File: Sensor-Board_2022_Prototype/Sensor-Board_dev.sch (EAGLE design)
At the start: 21 parts

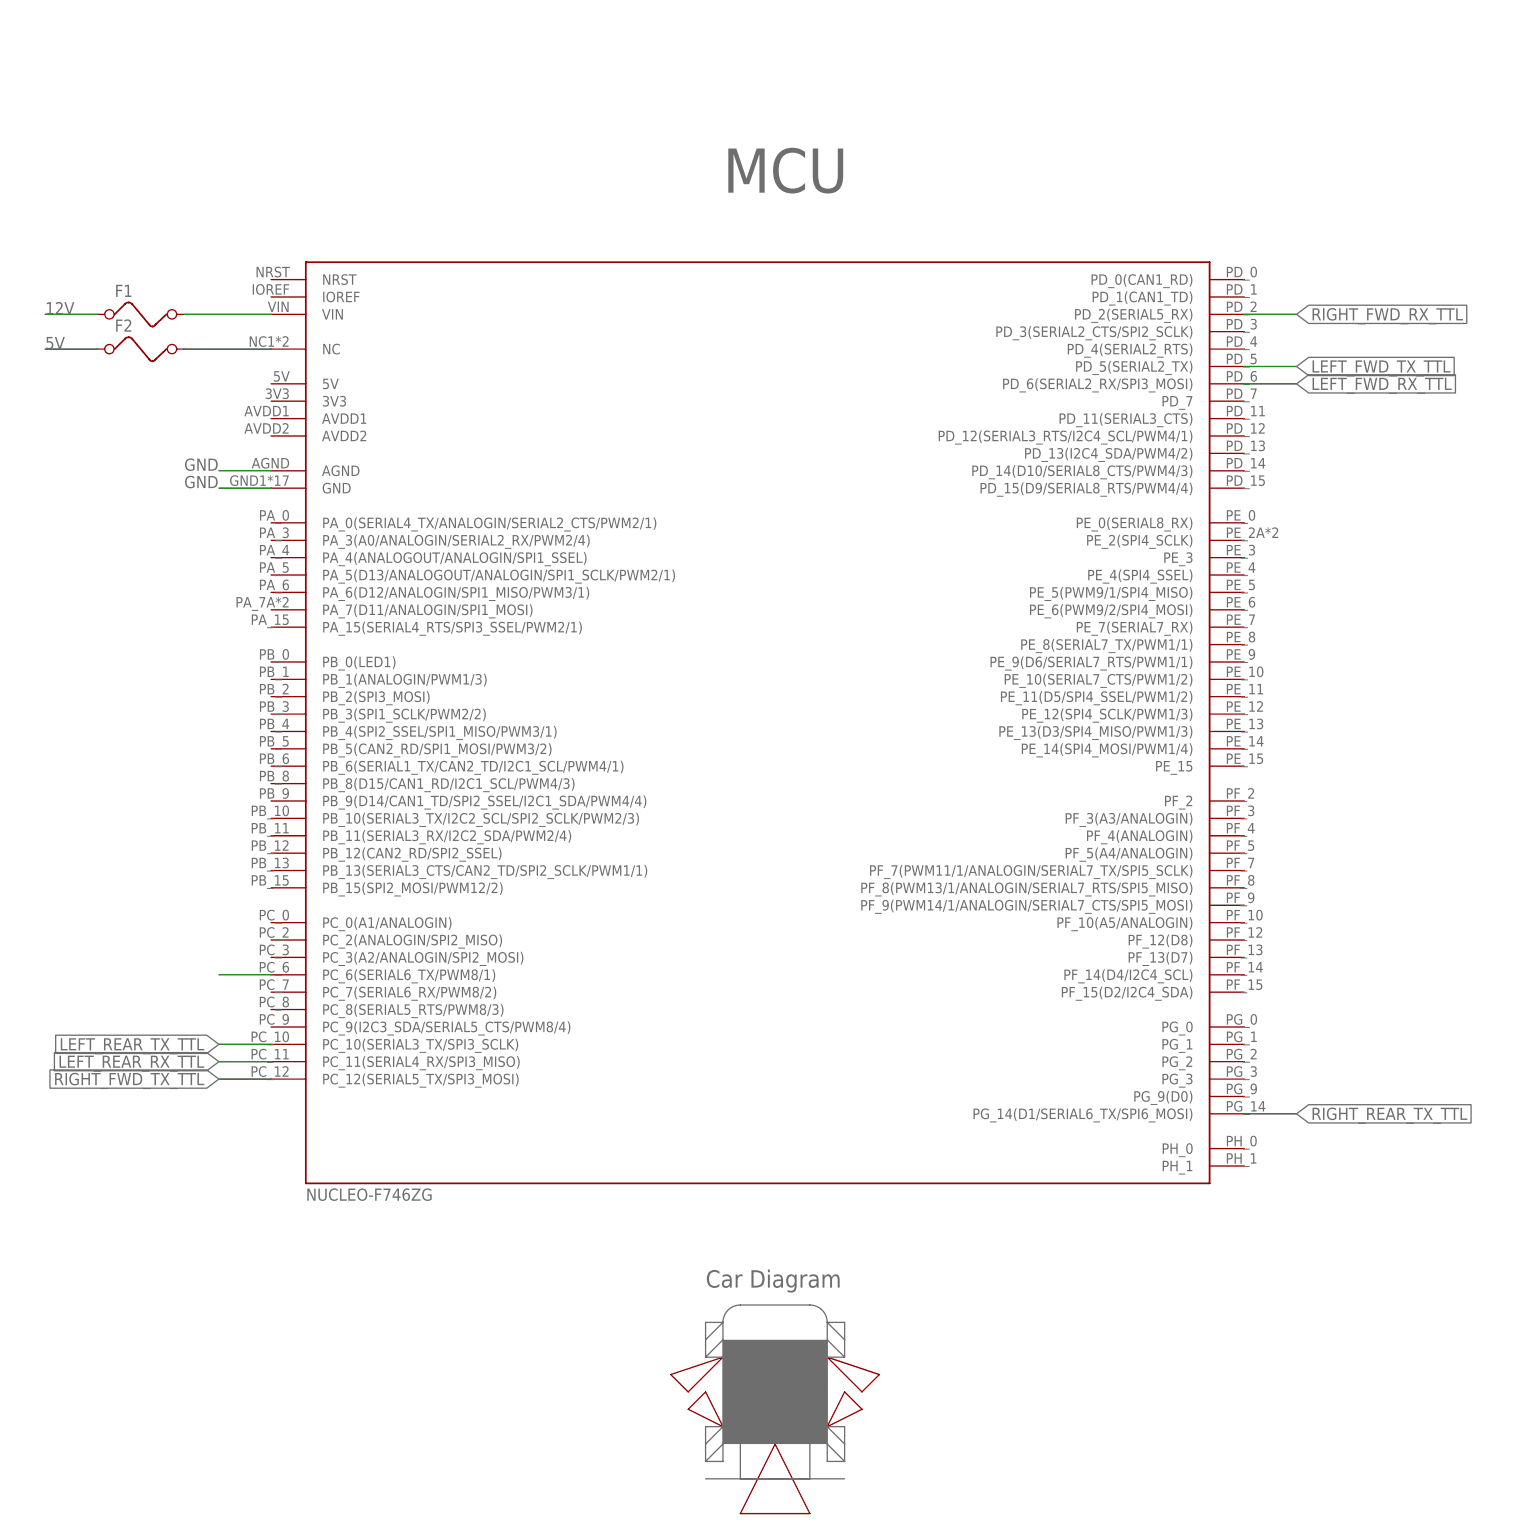
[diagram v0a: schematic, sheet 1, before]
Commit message: Added side signal labels
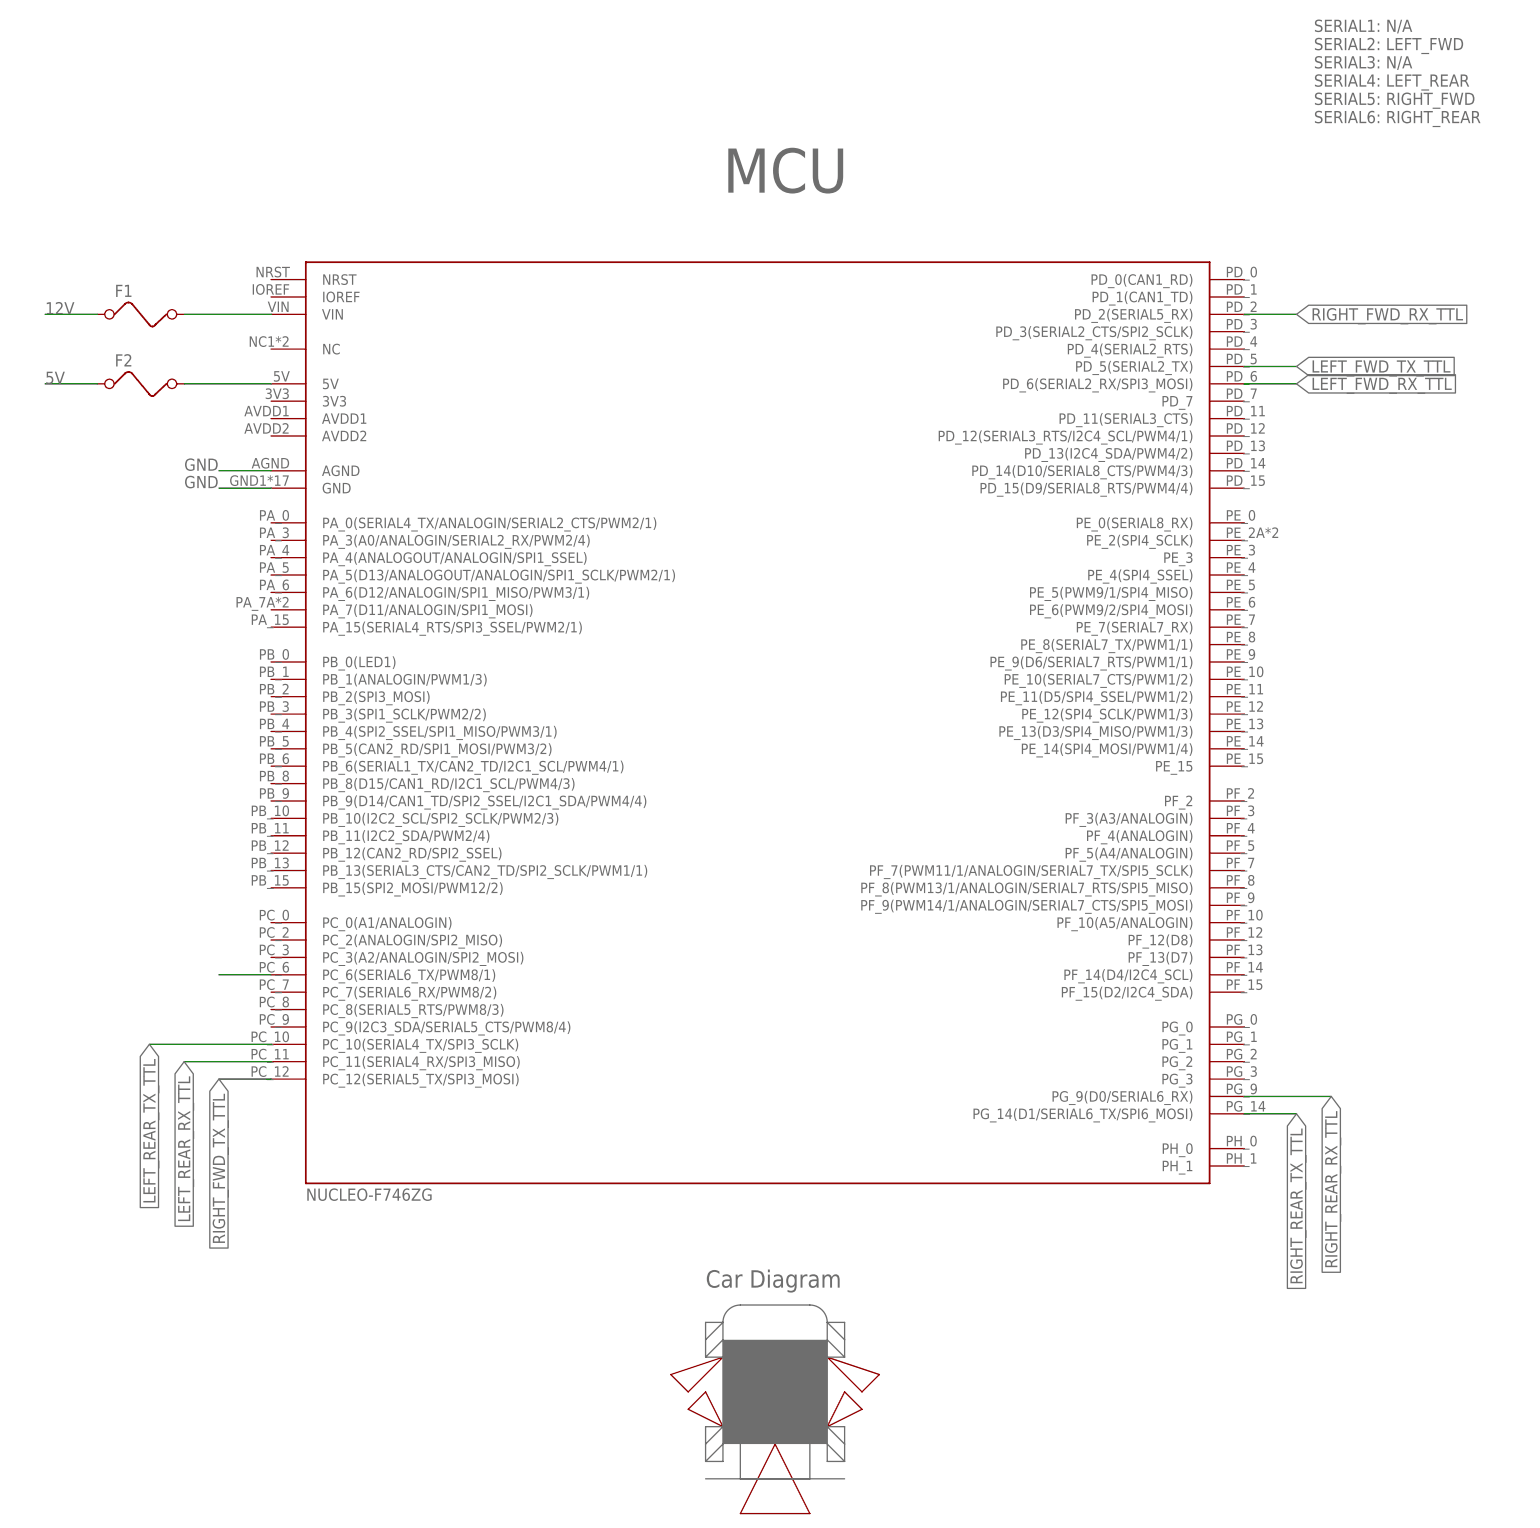
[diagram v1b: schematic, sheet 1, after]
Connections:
- net LEFT_REAR_TX_TTL: now also UC1.PC_10(SERIAL4_TX/SPI3_SCLK); no longer UC1.PC_10(SERIAL3_TX/SPI3_SCLK)
- net N$9: now also UC1.5V; no longer UC1.NC
- net RIGHT_REAR_RX_TTL: now also UC1.PG_9(D0/SERIAL6_RX)
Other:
- note added: "SERIAL1: N/A SERIAL2: LEFT_FWD SERIAL3: N/A SERIAL4: LEFT_REAR SERIAL5: RIGHT_FWD SERIAL6: RIGHT_REAR"
- moved on the sheet: F2
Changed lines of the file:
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@@
 <wire x1="160.02" y1="-5.08" x2="157.48" y2="-7.62" width="0.1524" layer="94"/>
 <text x="134.62" y="7.62" size="2.54" layer="95">Car Diagram</text>
+<text x="223.52" y="177.8" size="1.778" layer="95">SERIAL1: N/A
+SERIAL2: LEFT_FWD
+SERIAL3: N/A
+SERIAL4: LEFT_REAR
+SERIAL5: RIGHT_FWD
+SERIAL6: RIGHT_REAR</text>
 </plain>
 <instances>
@@
 <attribute name="VALUE" x="48.26" y="146.05" size="1.778" layer="96"/>
 </instance>
-<instance part="F2" gate="G$1" x="53.34" y="144.78" smashed="yes">
-<attribute name="NAME" x="48.26" y="147.32" size="1.778" layer="95"/>
-<attribute name="VALUE" x="48.26" y="140.97" size="1.778" layer="96"/>
+<instance part="F2" gate="G$1" x="53.34" y="139.7" smashed="yes">
+<attribute name="NAME" x="48.26" y="142.24" size="1.778" layer="95"/>
+<attribute name="VALUE" x="48.26" y="135.89" size="1.778" layer="96"/>
 </instance>
 <instance part="FRAME2" gate="G$1" x="-66.04" y="-58.42" smashed="yes"/>
@@
 <segment>
 <pinref part="F2" gate="G$1" pin="1"/>
-<wire x1="45.72" y1="144.78" x2="38.1" y2="144.78" width="0.1524" layer="91"/>
-<label x="38.1" y="144.78" size="1.778" layer="95"/>
+<wire x1="45.72" y1="139.7" x2="38.1" y2="139.7" width="0.1524" layer="91"/>
+<label x="38.1" y="139.7" size="1.778" layer="95"/>
 </segment>
 </net>
@@
 </segment>
 </net>
-<net name="N$9" class="0">
-<segment>
-<pinref part="UC1" gate="G$1" pin="NC"/>
-<wire x1="71.12" y1="144.78" x2="58.42" y2="144.78" width="0.1524" layer="91"/>
-<pinref part="F2" gate="G$1" pin="2"/>
-</segment>
-</net>
 <net name="LEFT_FWD_RX_TTL" class="0">
 <segment>
@@
 <segment>
 <pinref part="UC1" gate="G$1" pin="PC_11(SERIAL4_RX/SPI3_MISO)"/>
-<wire x1="71.12" y1="40.64" x2="63.5" y2="40.64" width="0.1524" layer="91"/>
-<label x="63.5" y="40.64" size="1.778" layer="95" rot="R180" xref="yes"/>
+<wire x1="71.12" y1="40.64" x2="58.42" y2="40.64" width="0.1524" layer="91"/>
+<label x="58.42" y="40.64" size="1.778" layer="95" rot="R270" xref="yes"/>
 </segment>
 </net>
 <net name="LEFT_REAR_TX_TTL" class="0">
 <segment>
-<pinref part="UC1" gate="G$1" pin="PC_10(SERIAL3_TX/SPI3_SCLK)"/>
-<wire x1="71.12" y1="43.18" x2="63.5" y2="43.18" width="0.1524" layer="91"/>
-<label x="63.5" y="43.18" size="1.778" layer="95" rot="R180" xref="yes"/>
+<pinref part="UC1" gate="G$1" pin="PC_10(SERIAL4_TX/SPI3_SCLK)"/>
+<wire x1="71.12" y1="43.18" x2="53.34" y2="43.18" width="0.1524" layer="91"/>
+<label x="53.34" y="43.18" size="1.778" layer="95" rot="R270" xref="yes"/>
 </segment>
 </net>
@@
 <pinref part="UC1" gate="G$1" pin="PC_12(SERIAL5_TX/SPI3_MOSI)"/>
 <wire x1="71.12" y1="38.1" x2="63.5" y2="38.1" width="0.1524" layer="91"/>
-<label x="63.5" y="38.1" size="1.778" layer="95" rot="R180" xref="yes"/>
+<label x="63.5" y="38.1" size="1.778" layer="95" rot="R270" xref="yes"/>
 </segment>
 </net>
@@
 <pinref part="UC1" gate="G$1" pin="PG_14(D1/SERIAL6_TX/SPI6_MOSI)"/>
 <wire x1="213.36" y1="33.02" x2="220.98" y2="33.02" width="0.1524" layer="91"/>
-<label x="220.98" y="33.02" size="1.778" layer="95" xref="yes"/>
+<label x="220.98" y="33.02" size="1.778" layer="95" rot="R270" xref="yes"/>
 </segment>
 </net>
@@
 <pinref part="UC1" gate="G$1" pin="PC_6(SERIAL6_TX/PWM8/1)"/>
 <wire x1="71.12" y1="53.34" x2="63.5" y2="53.34" width="0.1524" layer="91"/>
+</segment>
+</net>
+<net name="N$9" class="0">
+<segment>
+<pinref part="UC1" gate="G$1" pin="5V"/>
+<wire x1="71.12" y1="139.7" x2="58.42" y2="139.7" width="0.1524" layer="91"/>
+<pinref part="F2" gate="G$1" pin="2"/>
+</segment>
+</net>
+<net name="RIGHT_REAR_RX_TTL" class="0">
+<segment>
+<pinref part="UC1" gate="G$1" pin="PG_9(D0/SERIAL6_RX)"/>
+<wire x1="213.36" y1="35.56" x2="226.06" y2="35.56" width="0.1524" layer="91"/>
+<label x="226.06" y="35.56" size="1.778" layer="95" rot="R270" xref="yes"/>
 </segment>
 </net>
@@
 </drawing>
 <compatibility>
+<note version="6.3" minversion="6.2.2" severity="warning">
+Since Version 6.2.2 text objects can contain more than one line,
+which will not be processed correctly with this version.
+</note>
 <note version="8.3" severity="warning">
 Since Version 8.3, EAGLE supports URNs for individual library
